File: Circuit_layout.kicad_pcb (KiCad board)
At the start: 2 copper layers, 203.2 x 165.1 mm, 233 parts, among them IC4 TS431ILT, J1 TSV, J18 ICSP, J2 CoolingSystem, J21 Lights On Car, J24 Cockpit, J25 RJ11, J3 Pedal, J32 Conn_MC, J34 Can_Iso, J35 GLV_In, J36 GLV_Out, J4 Conn_01x08, J5 Testing Connector, J6 AIRs/SafetyLoop, J7 IMD, J8 DC_Relay, J9 PC_Relay, K1 APAN3105, K2 G2R-1A-DC24, Q1 ZVP0545G, Q2 MMBF170, Q3 ZVP1320F, Q4 STN3NF06L, Q5 SI1302DL-T1-E3, SW2 TS5A3159-Q1, SW4 SW_PUSH, U1 RDE03110S12, U10 MCP2551-I/SN, U11 TLP293, U12 TLP293, U13 REF3033, U14 Mounting_hole, U15 Mounting_hole, U16 MCP9700AT-H/TT, U17 Chassis Ground, U18 TS912, U19 74HC00, U2 MCP6002, U20 MC7805BDTRKG, U21 MCP6004, U22 TS372, U23 TLP293, U24 TLP293, U25 NCD9830DBR2G, U27 TLP293, U28 Mounting_hole, U3 MCP6004, U30 DAC5574IDGS, U31 TLP293, U32 TLP293, U37 TLP293, U4 ACPL-C870, U40 MCP6004, U41 PDQ10-Q24-D5-D, U42 LT1763CS8-3.3PBF, U5 SI8600AB-B-IS, U6 TS912, U7 MCP23016, U8 74ACT11030, U9 PIC32MZ2048EFM064-I/PT

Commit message: F2018 version 1 before review
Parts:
- removed G***: LOGO, custom_footprints:logo_lafayette_ece_20mmx7mm
- removed G***: LOGO, custom_footprints:peppa_pig_LOGO
- removed HIGH VOLTAGE: Symbol_HighVoltage_Type2_CopperTop_VerySmall, Symbols:Symbol_HighVoltage_Type2_CopperTop_VerySmall
- removed VAL: REF, custom_footprints:lafLogo
- added C14: 0.1u, Capacitors_SMD:C_0805_HandSoldering, F.Cu at (248.4, 152.4)
- added C17: 0.1u, Capacitors_SMD:C_0805_HandSoldering, F.Cu at (233.9, 126.2)
- added JP4: Jumper-Device, Pin_Headers:Pin_Header_Straight_1x02_Pitch2.54mm, F.Cu at (57.4, 165.9)
- added RV1: POT_TRIM, TC33X-2-103E:35WR, F.Cu at (123.3, 180.7)
- C1: value 0.47uF -> 0.47u; footprint custom_footprints:C_0805 -> Capacitors_SMD:C_0805
- C10, C11, C13, C15, C16, C18, C19, C22, C23, C24, C28, C29, C3, C30, C32, C34, C35, C36, C39, C4, C42, C43, C44, C45, C46, C47, C48, C53, C58, C6, C7, C8, C9: footprint custom_footprints:C_0805_HandSoldering -> Capacitors_SMD:C_0805_HandSoldering
- C12: value 0.33uF -> 0.33u; footprint custom_footprints:C_0805_HandSoldering -> Capacitors_SMD:C_0805_HandSoldering
- C2: value 4.7uF -> 4.7u; footprint custom_footprints:C_0805_HandSoldering -> Capacitors_SMD:C_0805_HandSoldering
- C5, C55: value 0.1uF -> 0.1u; footprint custom_footprints:C_0805_HandSoldering -> Capacitors_SMD:C_0805_HandSoldering
- C54: value 15uF -> 15u; footprint custom_footprints:C_0805_HandSoldering -> Capacitors_SMD:C_0805_HandSoldering
- C56, C57, C61: value 10uF -> 10u; footprint custom_footprints:C_0805_HandSoldering -> Capacitors_SMD:C_0805_HandSoldering
- C59, C60: value 1uF -> 1u; footprint custom_footprints:C_0805_HandSoldering -> Capacitors_SMD:C_0805_HandSoldering
- D1, D2, D3, D4, D6, D7: footprint custom_footprints:LED_0805_HandSoldering -> LEDs:LED_0805_HandSoldering
- D10: value TL431LP -> ATL431; footprint custom_footprints:SOT-23 -> custom_footprints:SOT-23_D10_special
- D5: value ~Throttle_PL -> Throttle_PL; footprint custom_footprints:LED_0805_HandSoldering -> LEDs:LED_0805_HandSoldering
- D8, D9: footprint custom_footprints:D_DO-41_SOD81_P7.62mm_Horizontal -> Diodes_THT:D_DO-41_SOD81_P7.62mm_Horizontal
- IC4: footprint custom_footprints:SOT-23-5_HandSoldering -> TO_SOT_Packages_SMD:SOT-23-5_HandSoldering
- J18, J21, J35, J36, J5: footprint custom_footprints:Molex_MiniFit-JR-5556-06A_2x03x4.20mm_Straight -> Connectors_Molex:Molex_MiniFit-JR-5556-06A_2x03x4.20mm_Straight
- J2, J32, J7: footprint custom_footprints:Molex_MiniFit-JR-5556-08A_2x04x4.20mm_Straight -> Connectors_Molex:Molex_MiniFit-JR-5556-08A_2x04x4.20mm_Straight
- J24, J3: footprint custom_footprints:Molex_MiniFit-JR-5556-10A_2x05x4.20mm_Straight -> Connectors_Molex:Molex_MiniFit-JR-5556-10A_2x05x4.20mm_Straight
- J34, J6: footprint custom_footprints:Molex_MiniFit-JR-5556-04A_2x02x4.20mm_Straight -> Connectors_Molex:Molex_MiniFit-JR-5556-04A_2x02x4.20mm_Straight
- J4: footprint custom_footprints:Pin_Header_Straight_1x08_Pitch2.54mm -> Pin_Headers:Pin_Header_Straight_1x08_Pitch2.54mm
- J8, J9: footprint custom_footprints:Molex_MiniFit-JR-5556-02A_2x01x4.20mm_Straight -> Connectors_Molex:Molex_MiniFit-JR-5556-02A_2x01x4.20mm_Straight
- JP1, JP3: footprint custom_footprints:Pin_Header_Straight_1x03_Pitch2.54mm -> Pin_Headers:Pin_Header_Straight_1x03_Pitch2.54mm
- JP2: footprint custom_footprints:Pin_Header_Straight_1x02_Pitch2.54mm -> Pin_Headers:Pin_Header_Straight_1x02_Pitch2.54mm
- K2: value G2R-1A-DC24 -> G6B-1174P-US-DC24; footprint custom_footprints:Relay_SPST_Finder_32.21-x300 -> custom_footprints:Relay_SPST_Finder_32.21-x300_special
- L1: footprint custom_footprints:L_0805_HandSoldering -> Inductors_SMD:L_0805_HandSoldering
- L2: footprint custom_footprints:L_0603_HandSoldering -> Inductors_SMD:L_0603_HandSoldering
- Q1: footprint custom_footprints:SOT-223-3_TabPin2 -> TO_SOT_Packages_SMD:SOT-223-3_TabPin2
- Q2, Q3, U13, U16: footprint custom_footprints:SOT-23 -> TO_SOT_Packages_SMD:SOT-23
- Q4: footprint custom_footprints:SOT-223 -> custom_footprints:SOT230P700X180-4N-speical
- Q5: footprint custom_footprints:SOT-323_SC-70_Handsoldering -> custom_footprints:SOT-323_SC-70_Handsoldering_special
- R1, R10, R11, R12, R13, R15, R17, R18, R19, R20, R21, R22, R23, R24, R25, R28, R29, R3, R30, R31, R32, R34, R35, R36, R37, R38, R39, R4, R40, R41, R42, R43, R44, R45, R47, R48, R49, R5, R50, R51, R52, R53, R55, R56, R57, R58, R59, R6, R60, R61, R62, R63, R64, R65, R66, R68, R69, R7, R70, R71, R72, R74, R76, R77, R78, R79, R8, R80, R81, R82, R83, R84, R85, R86, R87, R88, R9, R97: footprint custom_footprints:R_0805_HandSoldering -> Resistors_SMD:R_0805_HandSoldering
- R14, R16, R89, R90, R91, R92, R93, R94, R95, R96: value 10K -> 10k; footprint custom_footprints:R_0805_HandSoldering -> Resistors_SMD:R_0805_HandSoldering
- R2: value 95K -> 95k; footprint custom_footprints:R_0805_HandSoldering -> Resistors_SMD:R_0805_HandSoldering
- R26: value 1k -> 1K; footprint custom_footprints:R_0805_HandSoldering -> Resistors_SMD:R_0805_HandSoldering
- R27, R98: value 10k -> 10K; footprint custom_footprints:R_0805_HandSoldering -> Resistors_SMD:R_0805_HandSoldering
- R33, R73, R75: value 5K -> 5k; footprint custom_footprints:R_0805_HandSoldering -> Resistors_SMD:R_0805_HandSoldering
- R46: value 1K -> 1k; footprint custom_footprints:R_0805_HandSoldering -> Resistors_SMD:R_0805_HandSoldering
- R54: value 150 -> 2.4k; footprint custom_footprints:R_0805_HandSoldering -> Resistors_SMD:R_0805_HandSoldering
- R67: value 2.4K -> 2.4k; footprint custom_footprints:R_0805_HandSoldering -> Resistors_SMD:R_0805_HandSoldering
- SW2: footprint custom_footprints:SOT-23-6_Handsoldering -> TO_SOT_Packages_SMD:SOT-23-6_Handsoldering
- U11, U12, U23, U24, U27, U31, U32, U37: footprint custom_footprints:SOP-4_4.4x2.8mm_Pitch1.27mm -> Housings_SSOP:SOP-4_4.4x2.8mm_Pitch1.27mm
- U20: footprint custom_footprints:TO-252-3_TabPin4 -> TO_SOT_Packages_SMD:TO-252-3_TabPin4
- U7: footprint Housings_SOIC:SOIC-28W_7.5x17.9mm_Pitch1.27mm -> MCP23016-I_SO:SOIC127P1030X265-28N
- moved R33 56.3 mm to (104.6, 130.6)
- moved R70 2.67 mm to (98.3, 130.6)
- moved R47 1.65 mm to (92.5, 130.6)
- moved R27 1.42 mm to (118.1, 60.5)
- moved R98 1.42 mm to (110.6, 60.5)
- moved D10 0.83 mm to (117.4, 54.3), turned to 180 degrees
- moved R26 0.18 mm to (110.5, 55.2)
- turned C55 to 180 degrees
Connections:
- C55 pad 1: /+5HV -> /I/O_Ground
- C55 pad 2: /I/O_Ground -> /+5HV
- D10 pad 1: /BP_RTN -> Net-(D10-Pad1)
- D10 pad 2: Net-(D10-Pad1) -> /BP_RTN
- J32 pad 3: /I/O_Ground -> /Pre-Charge/I/O_ground
- J7 pad 1: /CH_gnd -> /BP_RTN
- J7 pad 3: /CH_gnd -> /BP_RTN
- J7 pad 4: /CH_gnd -> /BP_RTN
- JP3 pad 2: /I/O_Ground -> /Pre-Charge/I/O_ground
- Q3 pad 2: /Status Lights/RTDS -> /+24V
- Q3 pad 3: /+24V -> /Status Lights/RTDS
- R33 pad 1: Net-(R2-Pad2) -> /+5V
- R33 pad 2: Net-(R33-Pad2) -> /PC_ready
- R36 pad 2: /CH_gnd -> /BP_RTN
- R43 pad 2: /CH_gnd -> /BP_RTN
- R54 pad 1: /+5HV -> /Pre-Charge/IGNI_VCC
- U21 pad 8: Net-(R33-Pad2) -> Net-(RV1-Pad3)
- U21 pad 9: Net-(R33-Pad2) -> Net-(RV1-Pad3)
- U32 pad 4: /+5V -> /BP_RTN
- U40 pad 3: Net-(R33-Pad2) -> Net-(RV1-Pad3)
- U40 pad 6: Net-(R2-Pad2) -> Net-(RV1-Pad2)
- U7 pad 10: Net-(U7-Pad10) -> /BP_RTN
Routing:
- net /BP_RTN: track 1354.2 -> 1443.4 mm, vias 47 -> 49
- net Net-(RV1-Pad2): track 0.00 -> 69.8 mm, vias 0 -> 2
- net /Pre-Charge/IGNI_VCC: track 18.9 -> 69.2 mm, vias 0 -> 2
- net Net-(R2-Pad2): track 56.2 -> 11.6 mm
- net Net-(RV1-Pad3): track 0.00 -> 42.1 mm, vias 0 -> 5
- net /CH_gnd: track 234.8 -> 195.4 mm
- net Net-(R33-Pad2): track 34.0 -> 0.00 mm, vias 3 -> 0
- net /HV+: track 29.9 -> 51.5 mm
- net Net-(D7-Pad1): track 77.7 -> 97.6 mm, vias 4 -> 5
- net /+24V: track 502.8 -> 513.0 mm
- net /+5V: track 705.4 -> 695.8 mm
- net /IMD_Status: track 252.3 -> 243.2 mm
- net /HV-: track 54.0 -> 63.1 mm
- net /BP: track 209.0 -> 202.1 mm
- net /I/O_Ground: track 461.1 -> 466.7 mm
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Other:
- outline, holes or cut-outs redrawn
- board text added: "MC Jumper"
- board text added: "TSI Board Fall 2019 Version I by Feng Qiu Zhengxie Hu Phillip Harding"
- board text removed: "TSI Board 2019 Version II by X. Chen, T. Zhu and Y. Zhang Made in USA"

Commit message: backup; Add cooling power connector
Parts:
- added R99: 5k, Resistors_SMD:R_0805_HandSoldering, F.Cu at (270.0, -40.9)
- added U26: TLP293, Housings_SSOP:SOP-4_4.4x2.8mm_Pitch1.27mm, F.Cu at (200.9, -41.7)
- C14: value 0.1u -> 1u; footprint Capacitors_SMD:C_0805_HandSoldering -> Capacitors_THT:C_Rect_L18.0mm_W9.0mm_P15.00mm_FKS3_FKP3
- C17: value 0.1u -> 4.7u
- J2: footprint Connectors_Molex:Molex_MiniFit-JR-5556-08A_2x04x4.20mm_Straight -> Connectors_Molex:Molex_MiniFit-JR-5556-10A_2x05x4.20mm_Straight
- RV1: value POT_TRIM -> 3296W-1-103LF; footprint TC33X-2-103E:35WR -> Potentiometers:Potentiometer_Trimmer_Bourns_3296W
- moved RV1 6.17 mm to (119.4, 185.4), turned to 0 degrees
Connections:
- Q4 pad 4: (no net) -> /Pre-Charge/PC_Relay-
- R33 pad 2: /PC_ready -> Net-(R33-Pad2)
- U32 pad 3: /PC_ready -> /BP_RTN
- U32 pad 4: /BP_RTN -> /PC_ready
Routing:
- net Net-(RV1-Pad3): track 42.1 -> 58.3 mm
- net /Pre-Charge/PC_Relay-: track 61.8 -> 68.1 mm
- net Net-(R2-Pad2): track 11.6 -> 16.6 mm, vias 2 -> 0
- net /Status Lights/Drive_LED: track 125.1 -> 127.5 mm
- net /I/O_Ground: track 466.7 -> 468.9 mm
- net /+5HV: track 330.8 -> 329.4 mm
- net Net-(R56-Pad1): track 32.4 -> 31.3 mm
- net /Status Lights/TSAL_1: track 220.6 -> 219.7 mm
- net Net-(RV1-Pad2): track 69.8 -> 69.5 mm, vias 2 -> 1
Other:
- net class Default: clearance 0.2 -> 0.5
- rule trace_clearance: 0.2 -> 0.5

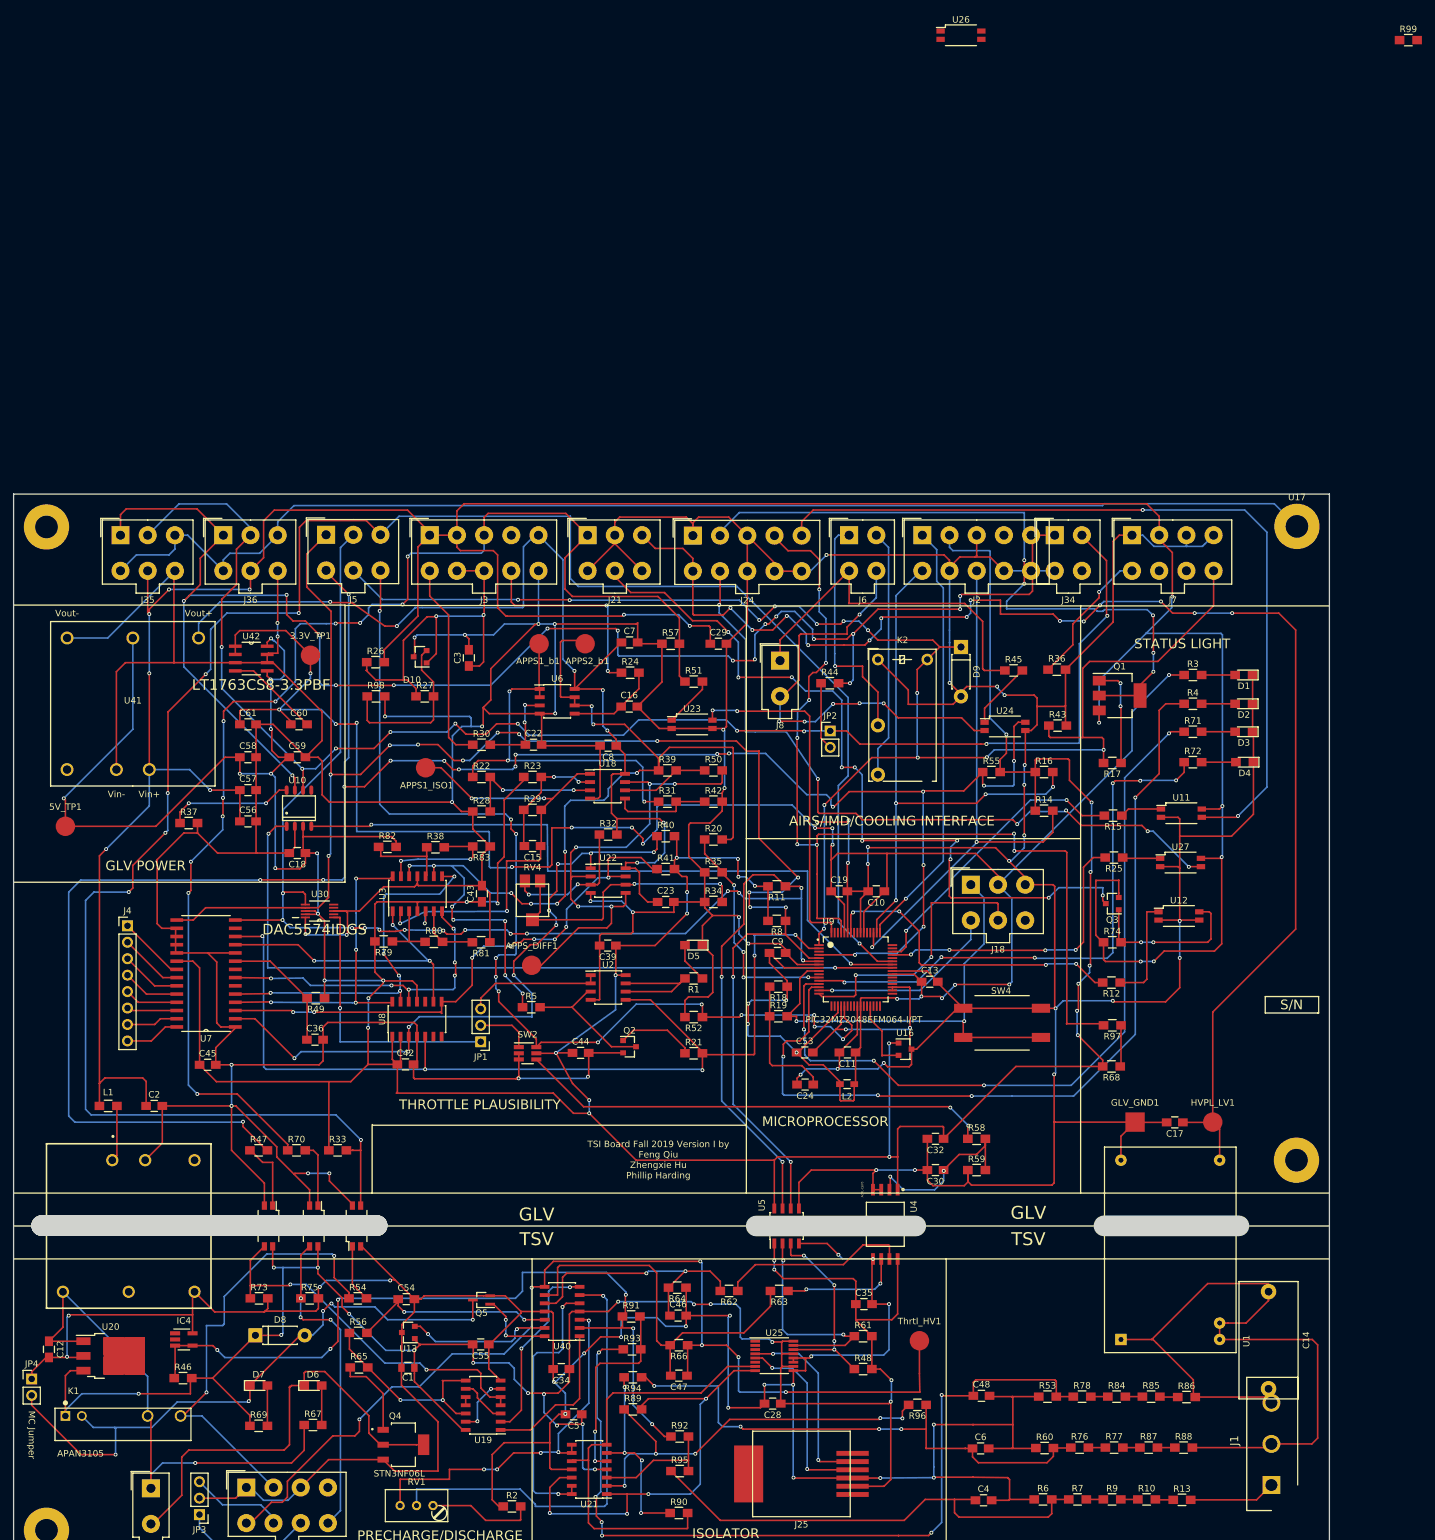
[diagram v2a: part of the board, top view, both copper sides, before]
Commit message: modify cooling power
relay added for cooling power control; reroute signals to PIC32 analog input
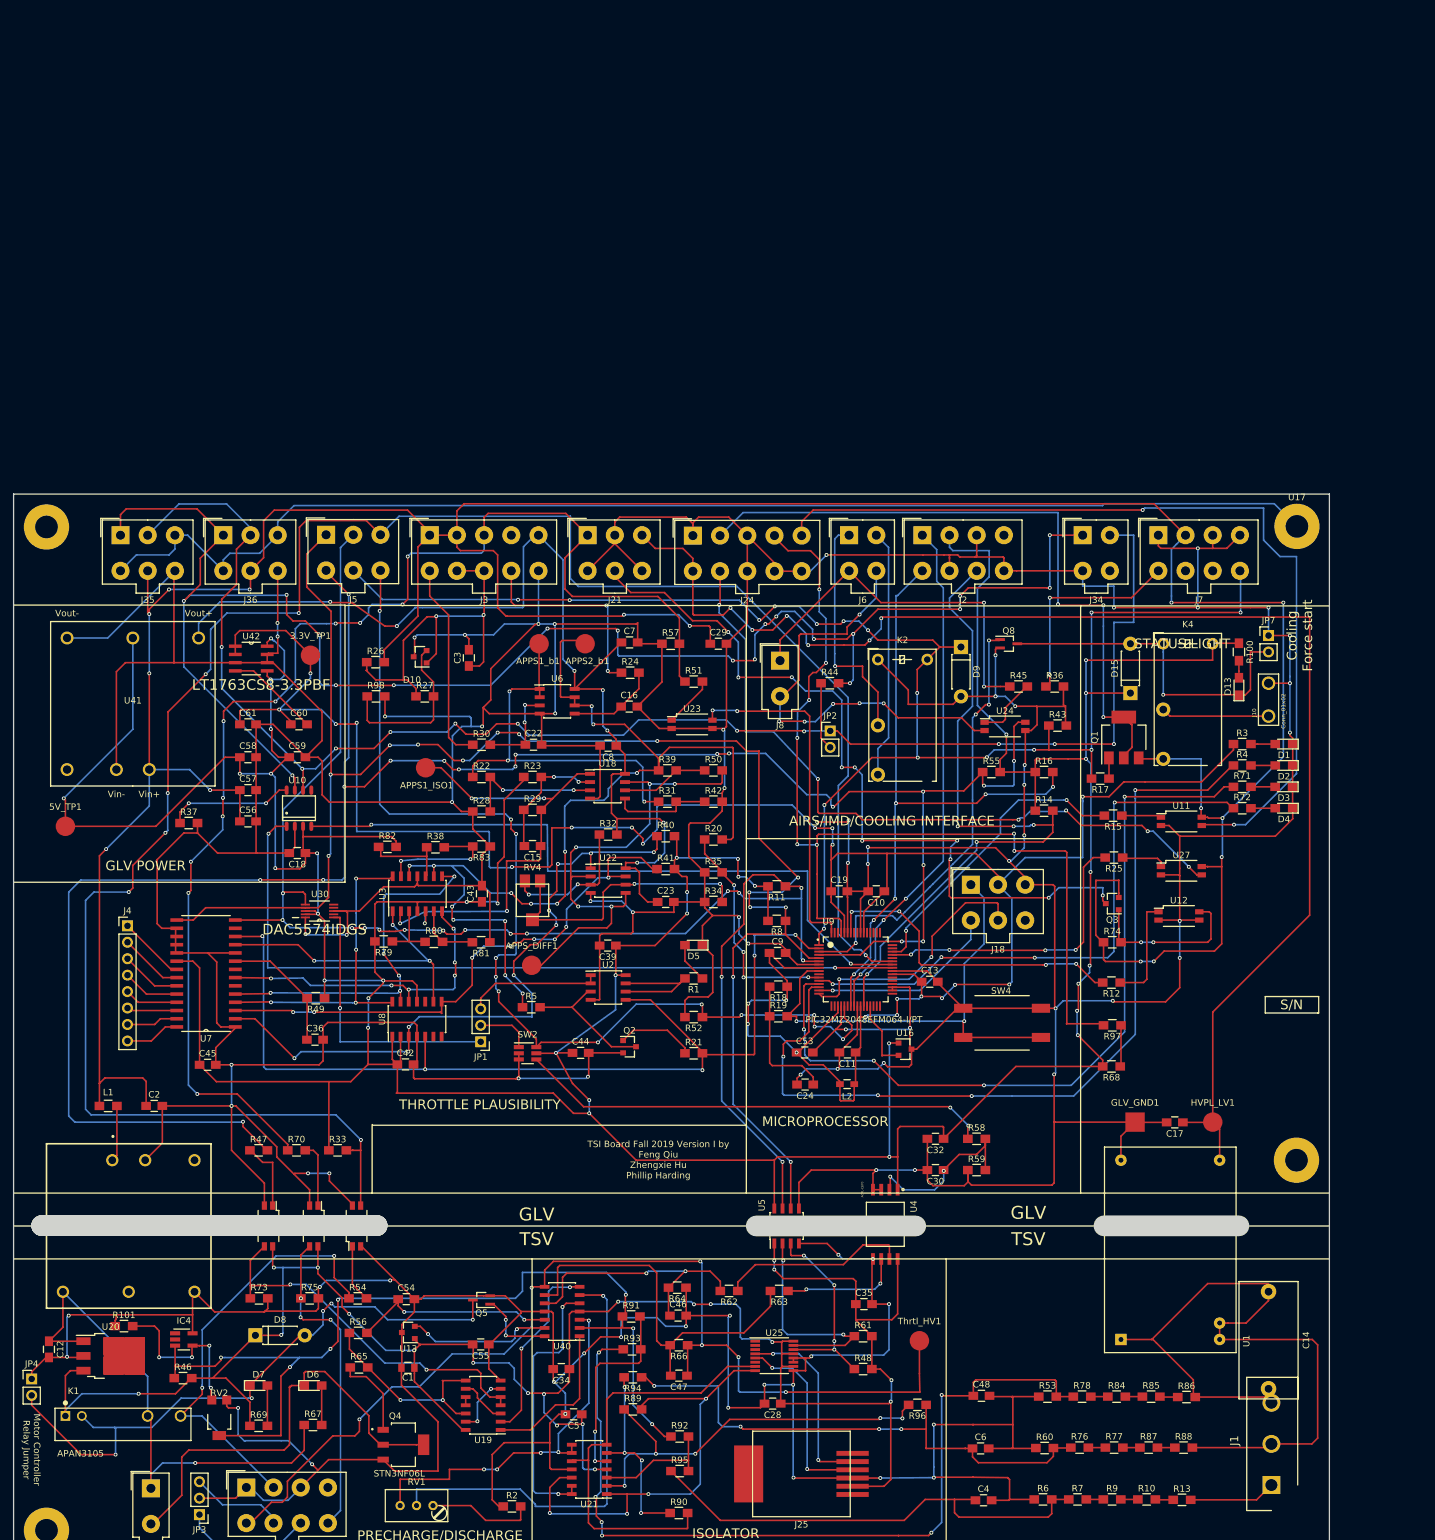
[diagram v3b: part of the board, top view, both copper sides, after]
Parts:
- removed R99: 5k, Resistors_SMD:R_0805_HandSoldering
- removed U26: TLP293, Housings_SSOP:SOP-4_4.4x2.8mm_Pitch1.27mm
- added D13: LED, LEDs:LED_0805_HandSoldering, F.Cu at (243.8, 58.9)
- added D15: 1N4001, Diodes_THT:D_DO-41_SOD81_P7.62mm_Horizontal, F.Cu at (227.1, 59.9)
- added J10: Conn_01x02, 1217861-1:TE_1217861-1, F.Cu at (248.4, 61.0)
- added JP7: Jumper-Device, Pin_Headers:Pin_Header_Straight_1x02_Pitch2.54mm, F.Cu at (248.4, 51.1)
- added K4: APAN3105, custom_footprints:Relay_SPST_Finder_32.21-x300_special, F.Cu at (232.2, 52.3)
- added Q8: SI1302DL-T1-E3, custom_footprints:SOT-323_SC-70_Handsoldering_special, F.Cu at (208.3, 52.3)
- added R100: 500, Resistors_SMD:R_0805_HandSoldering, F.Cu at (243.8, 53.6)
- added R101: 10k, Resistors_SMD:R_0805_HandSoldering, F.Cu at (71.7, 157.7)
- added RV2: POT_TRIM, custom_footprints:23BR10KLFTR, F.Cu at (86.4, 171.9)
- J2: footprint Connectors_Molex:Molex_MiniFit-JR-5556-10A_2x05x4.20mm_Straight -> Connectors_Molex:Molex_MiniFit-JR-5556-08A_2x04x4.20mm_Straight
- moved R3 13.1 mm to (244.3, 67.8)
- moved D1 12.3 mm to (250.8, 67.8)
- moved R4 12.2 mm to (244.3, 71.1)
- moved R71 11.4 mm to (244.3, 74.4)
- moved D2 11.4 mm to (250.8, 71.1)
- moved D3 10.5 mm to (250.8, 74.4)
- moved R72 10.4 mm to (244.3, 77.7)
- moved D4 9.35 mm to (250.8, 77.7)
- moved Q1 6.51 mm to (226.1, 66.8), turned to 90 degrees
- moved J34 4.32 mm to (219.7, 35.6)
- moved J7 4.06 mm to (231.4, 35.6)
- moved R17 3.05 mm to (222.4, 73.2)
- moved R36 2.62 mm to (215.4, 58.9)
- moved R45 2.59 mm to (209.8, 58.9)
- moved U27 1.28 mm to (234.9, 87.4)
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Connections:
- IC4 pad 4: /+1.24Vref -> Net-(IC4-Pad4)
- U9 pad 23: Net-(U9-Pad23) -> /CoolTemp_1
- U9 pad 24: Net-(U9-Pad24) -> /FlowRate
- U9 pad 27: Net-(U9-Pad27) -> /CoolTemp_2
- U9 pad 3: Net-(U9-Pad3) -> /Cooling_CTRL
- U9 pad 49: /FlowRate -> Net-(U9-Pad49)
- U9 pad 50: /CoolTemp_1 -> Net-(U9-Pad50)
- U9 pad 51: /CoolTemp_2 -> Net-(U9-Pad51)
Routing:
- net /Cooling_CTRL: track 0.00 -> 68.2 mm, vias 0 -> 4
- net Net-(D13-Pad1): track 0.00 -> 53.7 mm, vias 0 -> 1
- net /+5V: track 695.8 -> 747.2 mm, vias 34 -> 36
- net /BP_RTN: track 1443.4 -> 1470.7 mm, vias 49 -> 56
- net Net-(IC4-Pad4): track 0.00 -> 26.5 mm, vias 0 -> 4
- net /CoolTemp_2: track 83.0 -> 106.8 mm, vias 2 -> 5
- net /I/O_Ground: track 468.9 -> 492.3 mm, vias 21 -> 23
- net /+1.24Vref: track 121.5 -> 144.3 mm, vias 6 -> 7
- net /Cooling_power: track 0.00 -> 16.7 mm
- net /FlowRate: track 66.8 -> 79.8 mm, vias 1 -> 3
- net /CoolTemp_1: track 86.8 -> 99.8 mm, vias 4 -> 6
- net Net-(Q1-Pad1): track 15.8 -> 3.21 mm, vias 2 -> 0
- net /GLV Interface/IMD_MHS: track 21.7 -> 32.6 mm, vias 1 -> 2
- net /+24V: track 513.0 -> 523.0 mm, vias 14 -> 15
- net /Status Lights/Drive_LED: track 127.5 -> 136.9 mm
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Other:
- net class Default: clearance 0.5 -> 0.2
- rule trace_clearance: 0.5 -> 0.2
- board text added: "Cooling Force start"
- board text added: "Motor Controller Relay Jumper"
- board text removed: "MC Jumper"
